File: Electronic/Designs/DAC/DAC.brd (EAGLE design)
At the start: 50 x 50 mm, 37 parts

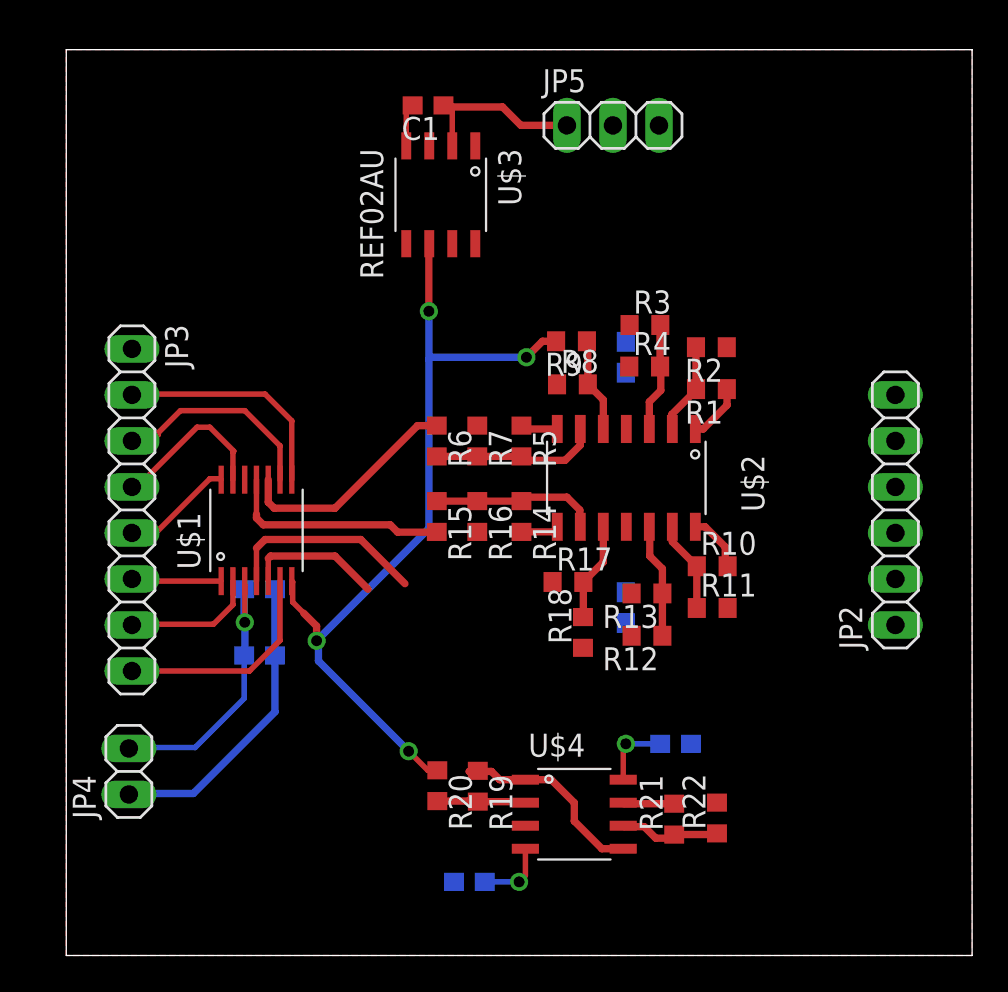
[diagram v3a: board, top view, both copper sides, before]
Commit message: Added to DAC board file
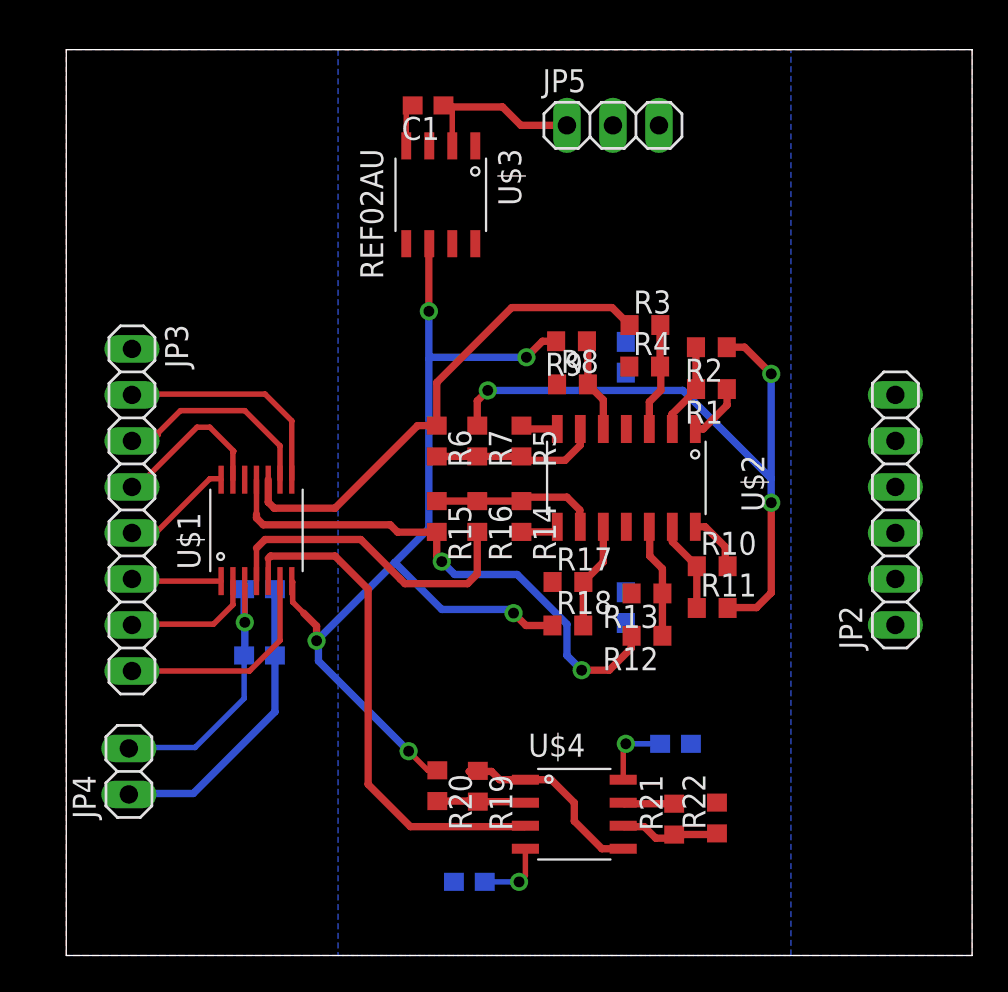
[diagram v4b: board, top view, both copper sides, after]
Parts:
- moved R18 0.92 mm to (27.7, 18.2), turned to 0 degrees
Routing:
- net Z: track 11.2 -> 55.5 mm, vias 0 -> 3
- net B: track 7.58 -> 28.0 mm
- net Y: track 12.4 -> 29.3 mm, vias 0 -> 2
- net X: track 12.6 -> 27.7 mm
- net VREF: track 46.0 -> 56.2 mm, vias 4 -> 5
- added copper zone on layer 16, net GND
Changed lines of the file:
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@@
 <element name="R16" library="resistor" package="R0603" value="10K" x="22.686" y="24.2316" rot="R270"/>
 <element name="R17" library="resistor" package="R0603" value="8k" x="27.6916" y="20.6164"/>
-<element name="R18" library="resistor" package="R0603" value="10k" x="28.5204" y="17.8308" rot="R90"/>
+<element name="R18" library="resistor" package="R0603" value="10k" x="27.686" y="18.2156"/>
 <element name="R2" library="resistor" package="R0603" value="10k" x="35.6076" y="33.5764" rot="R180"/>
 <element name="R3" library="resistor" package="R0603" value="10k" x="31.9404" y="34.8004"/>
@@
 <wire x1="7.0104" y1="8.9408" x2="3.5052" y2="8.9408" width="0.4064" layer="16"/>
 <wire x1="3.5052" y1="8.9408" x2="3.4544" y2="8.89" width="0.4064" layer="16"/>
+<polygon width="0.4064" layer="16">
+<vertex x="15" y="0"/>
+<vertex x="40" y="0"/>
+<vertex x="40" y="50"/>
+<vertex x="15" y="50"/>
+</polygon>
 <wire x1="31.0768" y1="32.5084" x2="30.8864" y2="33.87" width="0" layer="19" extent="1-16"/>
-<wire x1="30.8864" y1="18.3524" x2="31.2048" y2="19.986" width="0" layer="19" extent="1-16"/>
-<wire x1="34.4796" y1="11.684" x2="35.9176" y2="8.4396" width="0" layer="19" extent="1-16"/>
-<wire x1="21.4004" y1="4.064" x2="11.518" y2="13.4484" width="0" layer="19" extent="16-16"/>
 </signal>
 <signal name="XPOS">
@@
 <wire x1="20.0152" y1="35.56" x2="20.0152" y2="32.9184" width="0.4064" layer="16"/>
 <wire x1="20.0152" y1="32.9184" x2="20.0152" y2="23.5712" width="0.4064" layer="16"/>
-<wire x1="20.0152" y1="23.5712" x2="13.8176" y2="17.3736" width="0.4064" layer="16"/>
+<wire x1="20.0152" y1="23.5712" x2="18.1356" y2="21.6916" width="0.4064" layer="16"/>
 <via x="13.8176" y="17.3736" extent="1-16" drill="0.6"/>
+<wire x1="18.1356" y1="21.6916" x2="13.8176" y2="17.3736" width="0.4064" layer="16"/>
 <wire x1="13.8176" y1="17.3736" x2="13.8176" y2="18.1864" width="0.4064" layer="1"/>
 <wire x1="13.8176" y1="18.1864" x2="13.1064" y2="18.8976" width="0.4064" layer="1"/>
@@
 <wire x1="25.4" y1="33.02" x2="20.1168" y2="33.02" width="0.4064" layer="16"/>
 <wire x1="20.1168" y1="33.02" x2="20.0152" y2="32.9184" width="0.4064" layer="16"/>
-<wire x1="20.4808" y1="10.2228" x2="28.5204" y2="16.9808" width="0" layer="19" extent="1-1"/>
+<wire x1="26.836" y1="18.2156" x2="25.3708" y2="18.2156" width="0.4064" layer="1"/>
+<wire x1="25.3708" y1="18.2156" x2="24.6888" y2="18.8976" width="0.4064" layer="1"/>
+<via x="24.6888" y="18.8976" extent="1-16" drill="0.6" shape="square"/>
+<wire x1="24.6888" y1="18.8976" x2="24.4856" y2="19.1008" width="0.4064" layer="16"/>
+<wire x1="24.4856" y1="19.1008" x2="20.7264" y2="19.1008" width="0.4064" layer="16"/>
+<wire x1="20.7264" y1="19.1008" x2="18.1356" y2="21.6916" width="0.4064" layer="16"/>
 </signal>
 <signal name="Z">
@@
 <contactref element="U$1" pad="P$4"/>
 <wire x1="10.4984" y1="20.664" x2="10.4984" y2="22.4872" width="0.3048" layer="1"/>
-<wire x1="16.256" y1="22.9616" x2="18.6944" y2="20.5232" width="0.4064" layer="1"/>
+<wire x1="16.256" y1="22.9616" x2="18.4404" y2="20.7772" width="0.4064" layer="1"/>
 <wire x1="10.4984" y1="22.4872" x2="10.9728" y2="22.9616" width="0.4064" layer="1"/>
 <wire x1="10.9728" y1="22.9616" x2="16.256" y2="22.9616" width="0.4064" layer="1"/>
-<wire x1="36.504" y1="19.1808" x2="36.4576" y2="33.5764" width="0" layer="19" extent="1-1"/>
-<wire x1="22.686" y1="29.2472" x2="36.4576" y2="33.5764" width="0" layer="19" extent="1-1"/>
+<wire x1="36.4576" y1="33.5764" x2="37.442" y2="33.5764" width="0.4064" layer="1"/>
+<wire x1="37.442" y1="33.5764" x2="38.9128" y2="32.1056" width="0.4064" layer="1"/>
+<via x="38.9128" y="32.1056" extent="1-16" drill="0.6" shape="square"/>
+<wire x1="38.9128" y1="32.1056" x2="38.9128" y2="26.3144" width="0.4064" layer="16"/>
+<via x="38.9128" y="24.9936" extent="1-16" drill="0.6" shape="square"/>
+<wire x1="38.9128" y1="26.3144" x2="38.9128" y2="24.9936" width="0.4064" layer="16"/>
+<wire x1="38.1" y1="19.2024" x2="36.5256" y2="19.2024" width="0.4064" layer="1"/>
+<wire x1="36.5256" y1="19.2024" x2="36.504" y2="19.1808" width="0.4064" layer="1"/>
+<wire x1="22.686" y1="29.2472" x2="22.686" y2="30.6108" width="0.4064" layer="1"/>
+<wire x1="22.686" y1="30.6108" x2="23.2664" y2="31.1912" width="0.4064" layer="1"/>
+<via x="23.2664" y="31.1912" extent="1-16" drill="0.6" shape="square"/>
+<wire x1="23.2664" y1="31.1912" x2="34.036" y2="31.1912" width="0.4064" layer="16"/>
+<wire x1="34.036" y1="31.1912" x2="38.9128" y2="26.3144" width="0.4064" layer="16"/>
+<wire x1="38.1" y1="19.2024" x2="38.9128" y2="20.0152" width="0.4064" layer="1"/>
+<wire x1="38.9128" y1="20.0152" x2="38.9128" y2="24.9936" width="0.4064" layer="1"/>
+<wire x1="22.686" y1="23.3816" x2="22.686" y2="21.0604" width="0.4064" layer="1"/>
+<wire x1="22.686" y1="21.0604" x2="22.1488" y2="20.5232" width="0.4064" layer="1"/>
+<wire x1="22.1488" y1="20.5232" x2="18.6944" y2="20.5232" width="0.4064" layer="1"/>
+<wire x1="18.6944" y1="20.5232" x2="18.4404" y2="20.7772" width="0.4064" layer="1"/>
 <wire x1="22.686" y1="23.3816" x2="22.686" y2="29.2472" width="0" layer="19" extent="1-1"/>
-<wire x1="18.6944" y1="20.5232" x2="22.686" y2="23.3816" width="0" layer="19" extent="1-1"/>
 </signal>
 <signal name="X">
@@
 <wire x1="20.4508" y1="29.2472" x2="19.392" y2="29.2472" width="0.4064" layer="1"/>
 <wire x1="19.392" y1="29.2472" x2="14.8336" y2="24.6888" width="0.4064" layer="1"/>
-<wire x1="20.4508" y1="29.2472" x2="31.0904" y2="34.8004" width="0" layer="19" extent="1-1"/>
+<wire x1="20.4508" y1="29.2472" x2="20.4508" y2="31.6268" width="0.4064" layer="1"/>
+<wire x1="20.4508" y1="31.6268" x2="24.5872" y2="35.7632" width="0.4064" layer="1"/>
+<wire x1="24.5872" y1="35.7632" x2="30.1276" y2="35.7632" width="0.4064" layer="1"/>
+<wire x1="30.1276" y1="35.7632" x2="31.0904" y2="34.8004" width="0.4064" layer="1"/>
 </signal>
 <signal name="N$14">
@@
 <wire x1="18.288" y1="23.368" x2="20.4372" y2="23.368" width="0.4064" layer="1"/>
 <wire x1="20.4372" y1="23.368" x2="20.4508" y2="23.3816" width="0.4064" layer="1"/>
-<wire x1="20.4508" y1="23.3816" x2="31.2048" y2="17.6492" width="0" layer="19" extent="1-1"/>
+<wire x1="20.4508" y1="23.3816" x2="20.4508" y2="22.018" width="0.4064" layer="1"/>
+<wire x1="20.4508" y1="22.018" x2="20.7264" y2="21.7424" width="0.4064" layer="1"/>
+<via x="20.7264" y="21.7424" extent="1-16" drill="0.6" shape="square"/>
+<wire x1="20.7264" y1="21.7424" x2="21.4376" y2="21.0312" width="0.4064" layer="16"/>
+<wire x1="21.4376" y1="21.0312" x2="24.892" y2="21.0312" width="0.4064" layer="16"/>
+<wire x1="24.892" y1="21.0312" x2="27.6352" y2="18.288" width="0.4064" layer="16"/>
+<wire x1="27.6352" y1="18.288" x2="27.6352" y2="16.5608" width="0.4064" layer="16"/>
+<wire x1="27.6352" y1="16.5608" x2="28.448" y2="15.748" width="0.4064" layer="16"/>
+<via x="28.448" y="15.748" extent="1-16" drill="0.6" shape="square"/>
+<wire x1="28.448" y1="15.748" x2="29.972" y2="15.748" width="0.4064" layer="1"/>
+<wire x1="29.972" y1="15.748" x2="31.1912" y2="16.9672" width="0.4064" layer="1"/>
+<wire x1="31.1912" y1="16.9672" x2="31.1912" y2="17.6356" width="0.4064" layer="1"/>
+<wire x1="31.1912" y1="17.6356" x2="31.2048" y2="17.6492" width="0.4064" layer="1"/>
 </signal>
 <signal name="N$15">
@@
 <wire x1="29.6436" y1="21.7184" x2="28.5416" y2="20.6164" width="0.4064" layer="1"/>
 <wire x1="28.5416" y1="20.6164" x2="28.5416" y2="18.702" width="0.4064" layer="1"/>
-<wire x1="28.5416" y1="18.702" x2="28.5204" y2="18.6808" width="0.4064" layer="1"/>
+<wire x1="28.5416" y1="18.702" x2="28.536" y2="18.2156" width="0.4064" layer="1"/>
 </signal>
 <signal name="B">
@@
 <wire x1="11.2776" y1="22.0472" x2="11.1484" y2="21.918" width="0.4064" layer="1"/>
 <contactref element="U$4" pad="P$3"/>
-<wire x1="25.3416" y1="7.1628" x2="16.6624" y2="20.2184" width="0" layer="19" extent="1-1"/>
+<wire x1="16.6624" y1="20.2184" x2="16.6624" y2="9.4488" width="0.4064" layer="1"/>
+<wire x1="16.6624" y1="9.4488" x2="18.9992" y2="7.112" width="0.4064" layer="1"/>
+<wire x1="18.9992" y1="7.112" x2="25.2908" y2="7.112" width="0.4064" layer="1"/>
+<wire x1="25.2908" y1="7.112" x2="25.3416" y2="7.1628" width="0.4064" layer="1"/>
 </signal>
 <signal name="N$19">

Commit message: improved dac board layout
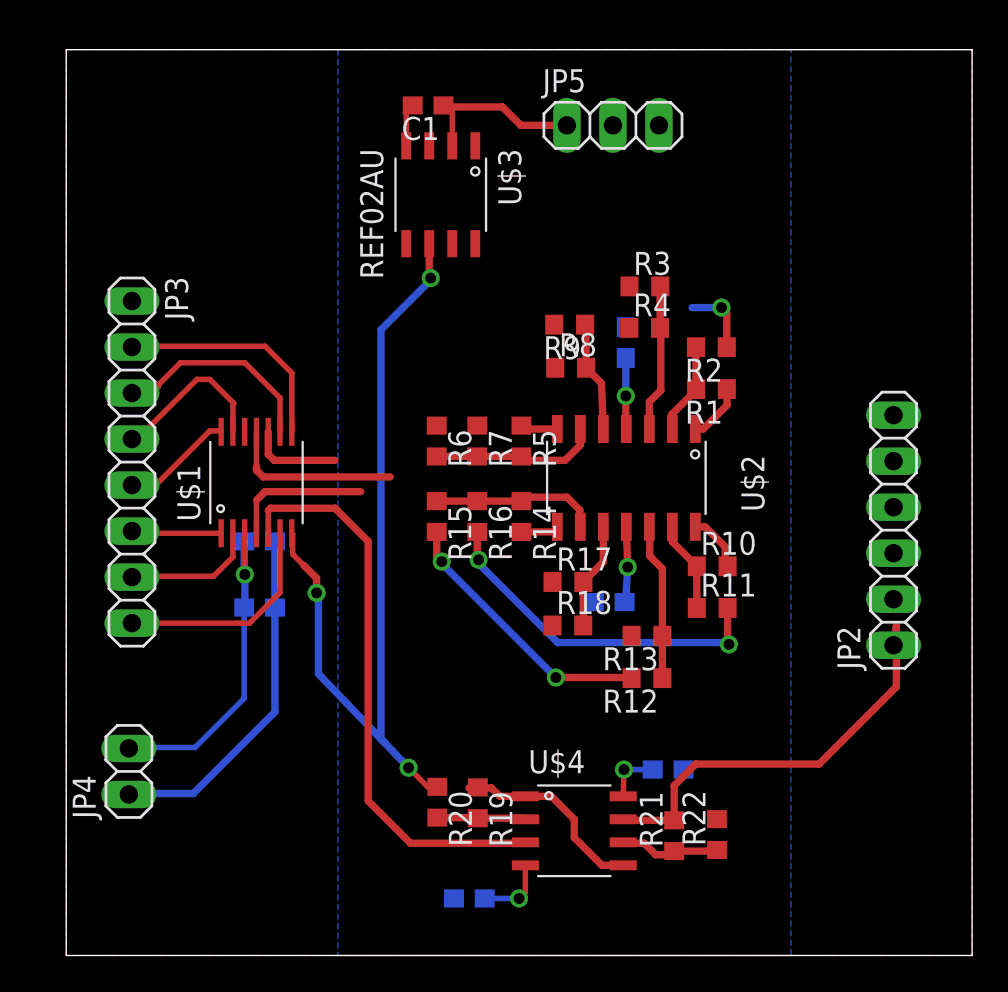
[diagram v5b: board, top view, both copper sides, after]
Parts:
- moved C4 14.6 mm to (30.9, 33.8), turned to 90 degrees
- moved C5 13.5 mm to (30.0, 19.5), turned to 0 degrees
- moved C2 2.64 mm to (10.7, 22.9)
- moved C3 2.64 mm to (10.7, 19.2)
- moved JP3 2.64 mm to (3.63, 27.2)
- moved U$1 2.64 mm to (10.5, 26.1)
- moved R12 2.34 mm to (32.1, 15.3)
- moved R13 2.34 mm to (32.1, 17.6)
- moved R4 2.13 mm to (31.9, 34.6)
- moved R3 2.13 mm to (31.9, 36.9)
- moved C7 1.48 mm to (33.2, 10.3)
- moved JP2 1.12 mm to (45.7, 23.5)
- moved R9 0.92 mm to (27.8, 34.8)
- moved R8 0.92 mm to (27.8, 32.4)
- moved R20 0.91 mm to (20.5, 8.46)
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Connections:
- net BIAS: now also JP2.1; no longer JP2.5
- net GND: now also JP2.2; no longer JP2.6
- net XNEG: now also JP2.6; no longer JP2.2
- net XPOS: now also JP2.5; no longer JP2.1
- net YNEG: now also JP2.3; no longer JP2.4
- net YPOS: now also JP2.4; no longer JP2.3
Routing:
- net Z: track 55.5 -> 31.2 mm
- net X: track 27.7 -> 5.07 mm
- net BIAS: track 2.84 -> 23.7 mm
- net VREF: track 56.2 -> 46.4 mm, vias 5 -> 3
- net Y: track 29.3 -> 24.6 mm
- net -15V: track 3.87 -> 8.11 mm, vias 1 -> 2
- net B: track 28.0 -> 31.6 mm
- net +15V: track 13.3 -> 16.6 mm, vias 1 -> 2
- net +5V: track 15.6 -> 18.2 mm
- net GND: track 19.4 -> 22.0 mm
- net N$14: track 6.31 -> 8.65 mm
- net N$5: track 6.02 -> 8.16 mm
- net N$7: track 5.22 -> 6.13 mm

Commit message: Added to dac pcb finished routing
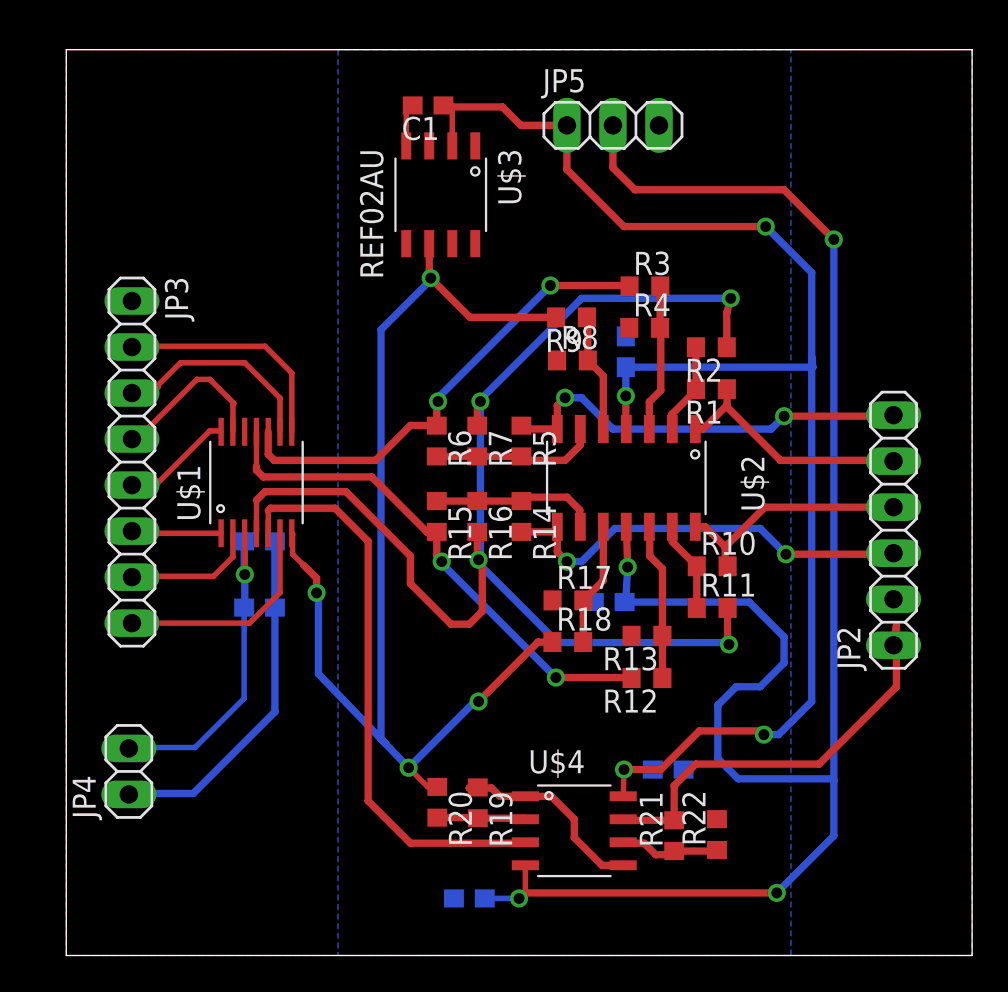
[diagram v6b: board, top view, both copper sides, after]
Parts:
- JP4: value (none) -> 5v
- JP5: value (none) -> 15v
- moved R17 1.02 mm to (27.7, 19.6)
- moved R18 0.91 mm to (27.7, 17.3)
- moved C4 0.51 mm to (30.9, 33.3)
- moved R8 0.42 mm to (27.9, 32.8)
- moved R9 0.42 mm to (27.9, 35.2)
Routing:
- net -15V: track 8.11 -> 101.5 mm, vias 2 -> 4
- net +15V: track 16.6 -> 81.0 mm, vias 2 -> 4
- net Z: track 31.2 -> 70.3 mm, vias 3 -> 4
- net YNEG: track 2.26 -> 23.5 mm, vias 0 -> 2
- net X: track 5.07 -> 26.2 mm, vias 0 -> 2
- net XNEG: track 2.19 -> 23.3 mm, vias 0 -> 2
- net VREF: track 46.4 -> 65.1 mm, vias 3 -> 4
- net XPOS: track 3.19 -> 13.7 mm
- net YPOS: track 3.40 -> 13.6 mm
- net Y: track 24.6 -> 28.4 mm
- net N$20: track 5.90 -> 6.82 mm

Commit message: increassed isolation distance to 12MIL on DAC board, this breaks alot of ground connections
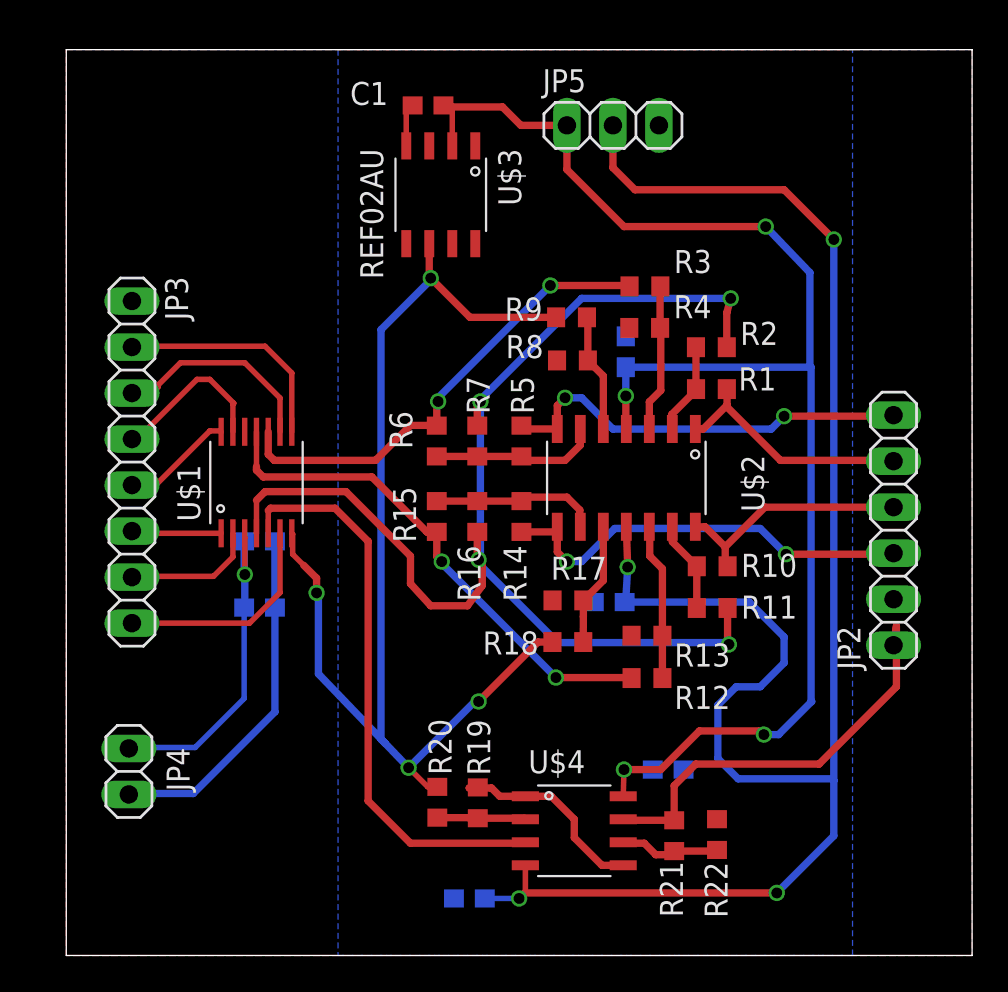
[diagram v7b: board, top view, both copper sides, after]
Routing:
- net Z: track 70.3 -> 68.7 mm
- net +15V: track 81.0 -> 80.3 mm
